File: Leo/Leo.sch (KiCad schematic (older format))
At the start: 64 parts, among them J1 CONN_POWER, J2 CONN_USB_B, J3 CONN_USB_MICRO, J4 CONN_MICROSD_47309-2651, P1 CONN_10, P10 CONN_1, P11 CONN_10, P12 CONN_10, P13 CONN_8, P14 CONN_8, P15 CONN_6, P16 CONN_6, P17 CONN_1, P18 CONN_3X2, P2 CONN_8, P3 CONN_8, P4 CONN_6, P5 CONN_1, P6 CONN_1, P7 CONN_1, P8 CONN_1, P9 CONN_1, U1 REGULATOR, U2 ATMEGA32U4, U3 REFERANCE-SO8, U4 MAX6369, U5 MCP7940, U6 REGULATOR, U7 74HC4050D, X2 RESONATOR

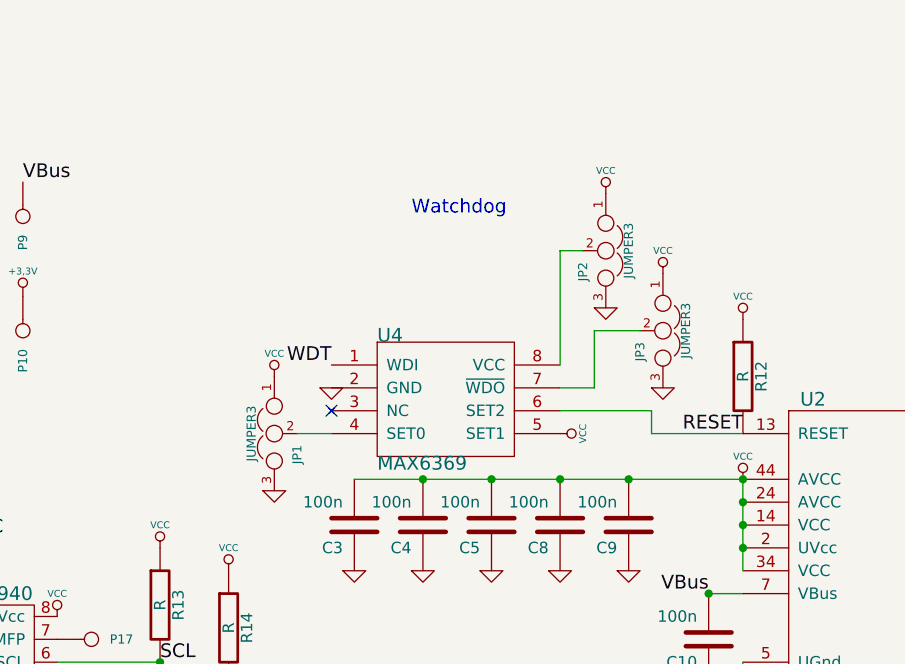
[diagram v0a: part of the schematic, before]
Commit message: Fixed MAX pinout, header spacing  and silkscreen
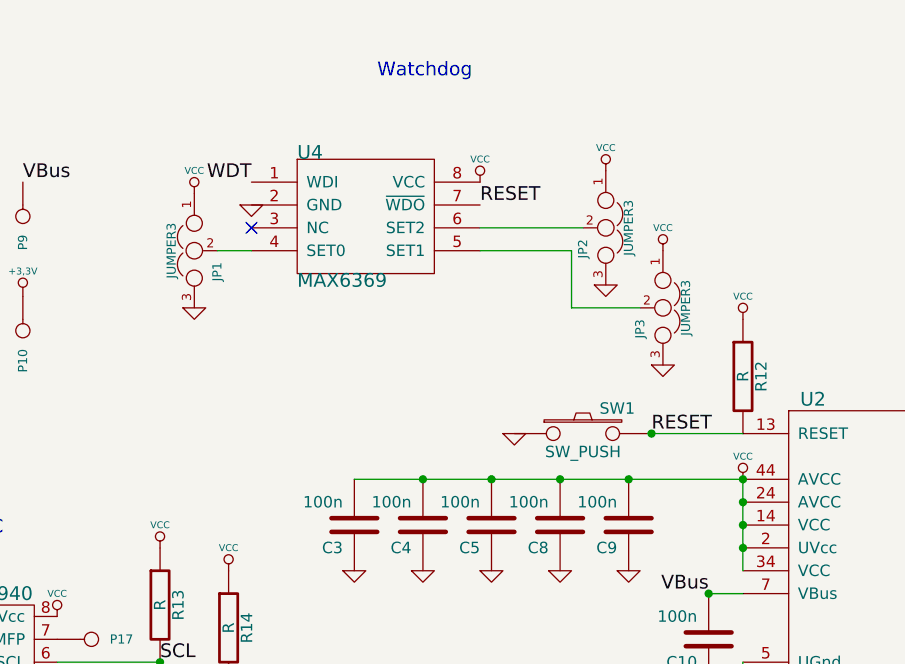
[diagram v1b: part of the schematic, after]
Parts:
- added SW1: SW_PUSH, symbol SW_PUSH
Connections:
- net GND: now also SW1.1
- net RESET: now also U4.7 (~WDO), SW1.2; no longer U4.6 (SET2)
- net VCC: now also U4.8 (VCC); no longer U4.5 (SET1)
- net at JP3.2: now also U4.5 (SET1); no longer U4.7 (~WDO)
- net at JP2.2: now also U4.6 (SET2); no longer U4.8 (VCC)
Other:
- moved on the sheet: JP1, JP2, JP3, U4
